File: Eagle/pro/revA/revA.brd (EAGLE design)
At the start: 100 x 100 mm, 4 parts

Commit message: mcu part
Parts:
- added U$1: ATSAM4LSAA-AUR, atmel:TQFP48
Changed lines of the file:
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@@
 <setting verticaltext="up"/>
 </settings>
-<grid distance="0.1" unitdist="mm" unit="mm" style="lines" multiple="1" display="yes" altdistance="0.025" altunitdist="inch" altunit="inch"/>
+<grid distance="0.1" unitdist="inch" unit="inch" style="lines" multiple="1" display="yes" altdistance="0.025" altunitdist="inch" altunit="inch"/>
 <layers>
 <layer number="1" name="Top" color="4" fill="1" visible="yes" active="yes"/>
@@
 <layer number="27" name="tValues" color="7" fill="1" visible="yes" active="yes"/>
 <layer number="28" name="bValues" color="7" fill="1" visible="yes" active="yes"/>
-<layer number="29" name="tStop" color="7" fill="3" visible="no" active="yes"/>
-<layer number="30" name="bStop" color="7" fill="6" visible="no" active="yes"/>
-<layer number="31" name="tCream" color="7" fill="4" visible="no" active="yes"/>
-<layer number="32" name="bCream" color="7" fill="5" visible="no" active="yes"/>
-<layer number="33" name="tFinish" color="6" fill="3" visible="no" active="yes"/>
-<layer number="34" name="bFinish" color="6" fill="6" visible="no" active="yes"/>
-<layer number="35" name="tGlue" color="7" fill="4" visible="no" active="yes"/>
-<layer number="36" name="bGlue" color="7" fill="5" visible="no" active="yes"/>
-<layer number="37" name="tTest" color="7" fill="1" visible="no" active="yes"/>
-<layer number="38" name="bTest" color="7" fill="1" visible="no" active="yes"/>
+<layer number="29" name="tStop" color="7" fill="3" visible="yes" active="yes"/>
+<layer number="30" name="bStop" color="7" fill="6" visible="yes" active="yes"/>
+<layer number="31" name="tCream" color="7" fill="4" visible="yes" active="yes"/>
+<layer number="32" name="bCream" color="7" fill="5" visible="yes" active="yes"/>
+<layer number="33" name="tFinish" color="6" fill="3" visible="yes" active="yes"/>
+<layer number="34" name="bFinish" color="6" fill="6" visible="yes" active="yes"/>
+<layer number="35" name="tGlue" color="7" fill="4" visible="yes" active="yes"/>
+<layer number="36" name="bGlue" color="7" fill="5" visible="yes" active="yes"/>
+<layer number="37" name="tTest" color="7" fill="1" visible="yes" active="yes"/>
+<layer number="38" name="bTest" color="7" fill="1" visible="yes" active="yes"/>
 <layer number="39" name="tKeepout" color="4" fill="11" visible="yes" active="yes"/>
 <layer number="40" name="bKeepout" color="1" fill="11" visible="yes" active="yes"/>
@@
 <layer number="42" name="bRestrict" color="1" fill="10" visible="yes" active="yes"/>
 <layer number="43" name="vRestrict" color="2" fill="10" visible="yes" active="yes"/>
-<layer number="44" name="Drills" color="7" fill="1" visible="no" active="yes"/>
+<layer number="44" name="Drills" color="7" fill="1" visible="yes" active="yes"/>
 <layer number="45" name="Holes" color="7" fill="1" visible="yes" active="yes"/>
-<layer number="46" name="Milling" color="3" fill="1" visible="no" active="yes"/>
-<layer number="47" name="Measures" color="7" fill="1" visible="no" active="yes"/>
+<layer number="46" name="Milling" color="3" fill="1" visible="yes" active="yes"/>
+<layer number="47" name="Measures" color="7" fill="1" visible="yes" active="yes"/>
 <layer number="48" name="Document" color="7" fill="1" visible="yes" active="yes"/>
 <layer number="49" name="Reference" color="7" fill="1" visible="yes" active="yes"/>
@@
 <element name="H3" library="holes" package="3,0-PAD" value="MOUNT-PAD-ROUND3.0" x="6" y="54"/>
 <element name="H4" library="holes" package="3,0-PAD" value="MOUNT-PAD-ROUND3.0" x="94" y="54"/>
+<element name="U$1" library="atmel" package="TQFP48" value="ATSAM4LSAA-AUR" x="27.8" y="17.1"/>
 </elements>
 <signals>

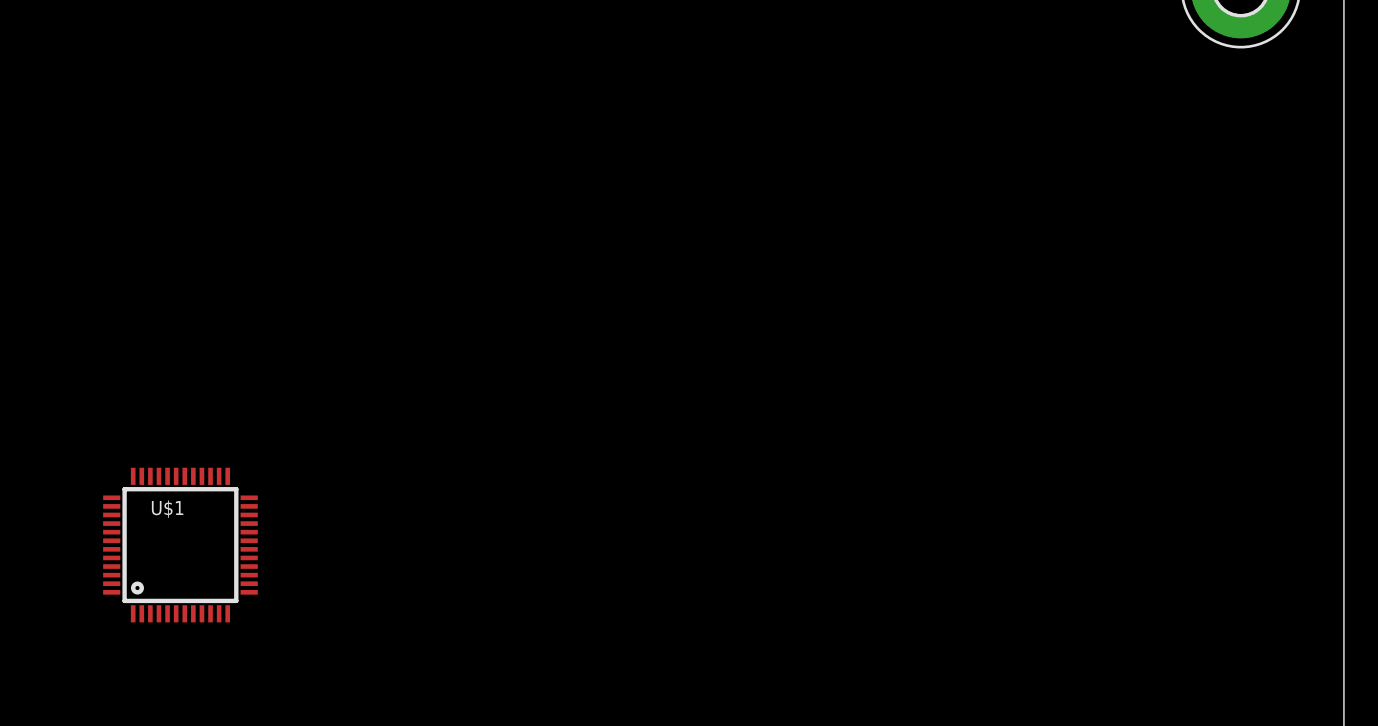
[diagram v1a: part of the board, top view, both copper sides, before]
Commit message: sort prog header
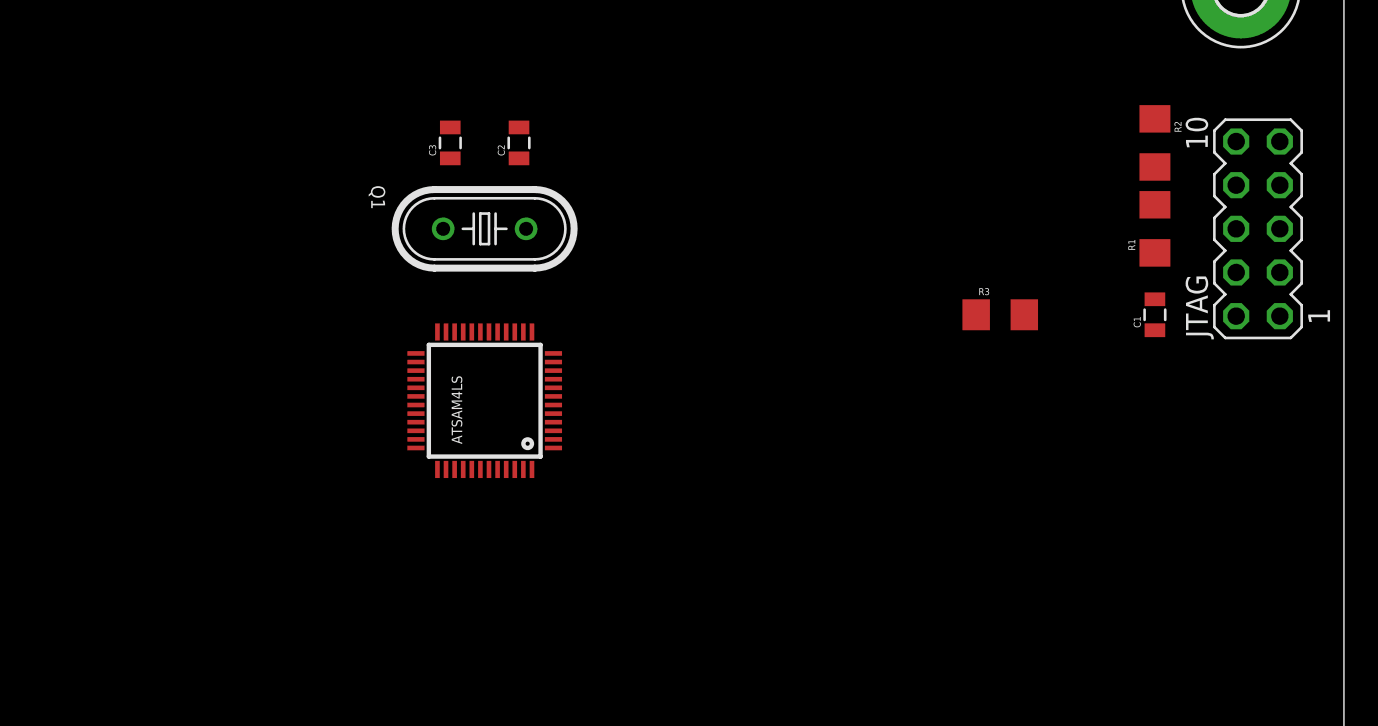
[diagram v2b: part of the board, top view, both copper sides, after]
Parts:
- removed U$1: ATSAM4LSAA-AUR, atmel:TQFP48
- added ATSAM4LS: ATSAM4LSAA-AUR, atmel:TQFP48
- added C1: 100nF, SparkFun:0805
- added C2, C3: 22pF, SparkFun:0805
- added JTAG: (no value), con-lstb:MA05-2
- added Q1: 20MHz, SparkFun:HC49U-V
- added R1, R2, R3: 100K, SparkFun:1206
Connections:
- new net 3.3V: C1.1, JTAG.1, R1.1, R2.1, R3.1
- new net GND: C1.2, C2.2, C3.2, JTAG.3, JTAG.5, JTAG.9
- new net N$1: ATSAM4LS.14, C3.1, Q1.2
- new net N$2: ATSAM4LS.13, C2.1, Q1.1
- new net NRESET: ATSAM4LS.4, JTAG.10
- new net TCK: ATSAM4LS.9, JTAG.4, R2.2
- new net TDI: ATSAM4LS.44, JTAG.8, R3.2
- new net TDO: ATSAM4LS.43, JTAG.6
- new net TMS: ATSAM4LS.10, JTAG.2, R1.2
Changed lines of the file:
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@@
 <setting verticaltext="up"/>
 </settings>
-<grid distance="0.1" unitdist="inch" unit="inch" style="lines" multiple="1" display="yes" altdistance="0.025" altunitdist="inch" altunit="inch"/>
+<grid distance="1" unitdist="mm" unit="mm" style="lines" multiple="1" display="yes" altdistance="0" altunitdist="inch" altunit="inch"/>
 <layers>
 <layer number="1" name="Top" color="4" fill="1" visible="yes" active="yes"/>
@@
 <layer number="48" name="Document" color="7" fill="1" visible="yes" active="yes"/>
 <layer number="49" name="Reference" color="7" fill="1" visible="yes" active="yes"/>
+<layer number="50" name="dxf" color="7" fill="1" visible="yes" active="yes"/>
 <layer number="51" name="tDocu" color="7" fill="1" visible="yes" active="yes"/>
 <layer number="52" name="bDocu" color="7" fill="1" visible="yes" active="yes"/>
+<layer number="53" name="tGND_GNDA" color="7" fill="9" visible="no" active="no"/>
+<layer number="54" name="bGND_GNDA" color="1" fill="9" visible="no" active="no"/>
+<layer number="56" name="wert" color="7" fill="1" visible="yes" active="yes"/>
 <layer number="91" name="Nets" color="2" fill="1" visible="no" active="no"/>
 <layer number="92" name="Busses" color="1" fill="1" visible="no" active="no"/>
@@
 <layer number="97" name="Info" color="7" fill="1" visible="no" active="no"/>
 <layer number="98" name="Guide" color="6" fill="1" visible="no" active="no"/>
+<layer number="100" name="Muster" color="7" fill="1" visible="no" active="no"/>
+<layer number="101" name="Patch_Top" color="12" fill="4" visible="yes" active="yes"/>
+<layer number="102" name="Vscore" color="7" fill="1" visible="yes" active="yes"/>
+<layer number="104" name="Name" color="7" fill="1" visible="yes" active="yes"/>
+<layer number="116" name="Patch_BOT" color="9" fill="4" visible="yes" active="yes"/>
+<layer number="121" name="_tsilk" color="7" fill="1" visible="yes" active="yes"/>
+<layer number="122" name="_bsilk" color="7" fill="1" visible="yes" active="yes"/>
+<layer number="151" name="HeatSink" color="7" fill="1" visible="yes" active="yes"/>
+<layer number="200" name="200bmp" color="1" fill="10" visible="yes" active="yes"/>
+<layer number="201" name="201bmp" color="2" fill="10" visible="yes" active="yes"/>
+<layer number="202" name="202bmp" color="3" fill="10" visible="yes" active="yes"/>
+<layer number="203" name="203bmp" color="4" fill="10" visible="yes" active="yes"/>
+<layer number="204" name="204bmp" color="5" fill="10" visible="yes" active="yes"/>
+<layer number="205" name="205bmp" color="6" fill="10" visible="yes" active="yes"/>
+<layer number="206" name="206bmp" color="7" fill="10" visible="yes" active="yes"/>
+<layer number="207" name="207bmp" color="8" fill="10" visible="yes" active="yes"/>
+<layer number="208" name="208bmp" color="9" fill="10" visible="yes" active="yes"/>
+<layer number="250" name="Descript" color="3" fill="1" visible="no" active="no"/>
+<layer number="251" name="SMDround" color="12" fill="11" visible="no" active="no"/>
+<layer number="254" name="cooling" color="7" fill="1" visible="yes" active="yes"/>
 </layers>
 <board>
@@
 <element name="H3" library="holes" package="3,0-PAD" value="MOUNT-PAD-ROUND3.0" x="6" y="54"/>
 <element name="H4" library="holes" package="3,0-PAD" value="MOUNT-PAD-ROUND3.0" x="94" y="54"/>
-<element name="U$1" library="atmel" package="TQFP48" value="ATSAM4LSAA-AUR" x="27.8" y="17.1"/>
+<element name="ATSAM4LS" library="atmel" package="TQFP48" value="ATSAM4LSAA-AUR" x="50" y="30" rot="R90"/>
+<element name="Q1" library="SparkFun" package="HC49U-V" value="20MHz" x="50" y="40" rot="R180"/>
+<element name="JTAG" library="con-lstb" package="MA05-2" value="" x="95" y="40" rot="R90">
+<attribute name="OC_NEWARK" value="unknown" x="95" y="40" size="1.778" layer="27" rot="R90" display="off"/>
+<attribute name="MPN" value="" x="95" y="40" size="1.778" layer="27" rot="R90" display="off"/>
+<attribute name="MF" value="" x="95" y="40" size="1.778" layer="27" rot="R90" display="off"/>
+<attribute name="OC_FARNELL" value="unknown" x="95" y="40" size="1.778" layer="27" rot="R90" display="off"/>
+</element>
+<element name="C1" library="SparkFun" package="0805" value="100nF" x="89" y="35" rot="R90"/>
+<element name="R1" library="SparkFun" package="1206" value="100K" x="89" y="40" rot="R90"/>
+<element name="R2" library="SparkFun" package="1206" value="100K" x="89" y="45" rot="R270"/>
+<element name="R3" library="SparkFun" package="1206" value="100K" x="80" y="35"/>
+<element name="C2" library="SparkFun" package="0805" value="22pF" x="52" y="45" rot="R90"/>
+<element name="C3" library="SparkFun" package="0805" value="22pF" x="48" y="45" rot="R90"/>
 </elements>
 <signals>
+<signal name="N$2">
+<contactref element="ATSAM4LS" pad="13"/>
+<contactref element="Q1" pad="1"/>
+<contactref element="C2" pad="1"/>
+<wire x1="52.413" y1="40" x2="52" y2="44.1" width="0" layer="19" extent="1-1"/>
+<wire x1="52.75290625" y1="33.9991125" x2="52.413" y2="40" width="0" layer="19" extent="1-1"/>
+</signal>
+<signal name="3.3V">
+<contactref element="R1" pad="1"/>
+<contactref element="R2" pad="1"/>
+<contactref element="JTAG" pad="1"/>
+<contactref element="C1" pad="1"/>
+<contactref element="R3" pad="1"/>
+<wire x1="89" y1="38.6" x2="89" y2="46.4" width="0" layer="19" extent="1-1"/>
+<wire x1="89" y1="34.1" x2="89" y2="38.6" width="0" layer="19" extent="1-1"/>
+<wire x1="96.27" y1="34.92" x2="89" y2="34.1" width="0" layer="19" extent="1-1"/>
+<wire x1="78.6" y1="35" x2="89" y2="34.1" width="0" layer="19" extent="1-1"/>
+</signal>
+<signal name="TMS">
+<contactref element="JTAG" pad="2"/>
+<contactref element="ATSAM4LS" pad="10"/>
+<contactref element="R1" pad="2"/>
+<wire x1="93.73" y1="34.92" x2="89" y2="41.4" width="0" layer="19" extent="1-1"/>
+<wire x1="54.00290625" y1="31.7491125" x2="89" y2="41.4" width="0" layer="19" extent="1-1"/>
+</signal>
+<signal name="TCK">
+<contactref element="JTAG" pad="4"/>
+<contactref element="R2" pad="2"/>
+<contactref element="ATSAM4LS" pad="9"/>
+<wire x1="93.73" y1="37.46" x2="89" y2="43.6" width="0" layer="19" extent="1-1"/>
+<wire x1="54.00290625" y1="31.2491125" x2="89" y2="43.6" width="0" layer="19" extent="1-1"/>
+</signal>
+<signal name="NRESET">
+<contactref element="ATSAM4LS" pad="4"/>
+<contactref element="JTAG" pad="10"/>
+<wire x1="54.00290625" y1="28.7491125" x2="93.73" y2="45.08" width="0" layer="19" extent="1-1"/>
+</signal>
+<signal name="TDO">
+<contactref element="JTAG" pad="6"/>
+<contactref element="ATSAM4LS" pad="43"/>
+<wire x1="50.25290625" y1="25.9991125" x2="93.73" y2="40" width="0" layer="19" extent="1-1"/>
+</signal>
+<signal name="TDI">
+<contactref element="JTAG" pad="8"/>
+<contactref element="ATSAM4LS" pad="44"/>
+<contactref element="R3" pad="2"/>
+<wire x1="81.4" y1="35" x2="93.73" y2="42.54" width="0" layer="19" extent="1-1"/>
+<wire x1="50.75290625" y1="25.9991125" x2="81.4" y2="35" width="0" layer="19" extent="1-1"/>
+</signal>
+<signal name="GND">
+<contactref element="C1" pad="2"/>
+<contactref element="JTAG" pad="5"/>
+<contactref element="JTAG" pad="9"/>
+<contactref element="JTAG" pad="3"/>
+<contactref element="C3" pad="2"/>
+<contactref element="C2" pad="2"/>
+<wire x1="96.27" y1="40" x2="96.27" y2="45.08" width="0" layer="19" extent="1-1"/>
+<wire x1="96.27" y1="37.46" x2="96.27" y2="40" width="0" layer="19" extent="1-1"/>
+<wire x1="89" y1="35.9" x2="96.27" y2="37.46" width="0" layer="19" extent="1-1"/>
+<wire x1="52" y1="45.9" x2="89" y2="35.9" width="0" layer="19" extent="1-1"/>
+<wire x1="48" y1="45.9" x2="52" y2="45.9" width="0" layer="19" extent="1-1"/>
+</signal>
+<signal name="N$1">
+<contactref element="Q1" pad="2"/>
+<contactref element="ATSAM4LS" pad="14"/>
+<contactref element="C3" pad="1"/>
+<wire x1="47.587" y1="40" x2="48" y2="44.1" width="0" layer="19" extent="1-1"/>
+<wire x1="52.25290625" y1="33.9991125" x2="47.587" y2="40" width="0" layer="19" extent="1-1"/>
+</signal>
 </signals>
 </board>

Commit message: op amps
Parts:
- added C4, C6: 22pF, SparkFun:0805
- added R10, R4, R6, R7, R8, R9: 100K, SparkFun:1206
- added U$1, U$2: LM393, SparkFun:SO08
- added U$3: AUDIO-JACKPTH, SparkFun:AUDIO-JACK
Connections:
- new net AUDIO_LEFT: ATSAM4LS.11, R4.2, U$1.1
- new net AUDIO_RIGHT: ATSAM4LS.12, R9.2, U$1.7
- new net N$10: U$1.4, U$2.4
- new net N$11: U$1.8, U$2.8
- new net N$12: U$2.3, U$3.2
- new net N$3: U$2.5, U$3.5
- new net N$4: R4.1, R6.2, U$1.2
- new net N$5: C6.1, R8.1, U$1.5
- new net N$6: C4.1, R7.1, U$1.3
- new net N$7: R8.2, U$2.6, U$2.7
- new net N$8: R7.2, U$2.1, U$2.2
- new net N$9: R10.2, R9.1, U$1.6
- net GND: now also C4.2, C6.2, R10.1, R6.1, U$3.1
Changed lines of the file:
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@@
 <element name="C2" library="SparkFun" package="0805" value="22pF" x="52" y="45" rot="R90"/>
 <element name="C3" library="SparkFun" package="0805" value="22pF" x="48" y="45" rot="R90"/>
+<element name="U$1" library="SparkFun" package="SO08" value="LM393" x="70" y="29"/>
+<element name="R4" library="SparkFun" package="1206" value="100K" x="55" y="16"/>
+<element name="R6" library="SparkFun" package="1206" value="100K" x="45" y="18"/>
+<element name="R7" library="SparkFun" package="1206" value="100K" x="78" y="16"/>
+<element name="C4" library="SparkFun" package="0805" value="22pF" x="73" y="14" rot="R90"/>
+<element name="R8" library="SparkFun" package="1206" value="100K" x="78" y="31"/>
+<element name="C6" library="SparkFun" package="0805" value="22pF" x="63" y="23"/>
+<element name="R9" library="SparkFun" package="1206" value="100K" x="67" y="41"/>
+<element name="R10" library="SparkFun" package="1206" value="100K" x="84" y="29" rot="R90"/>
+<element name="U$2" library="SparkFun" package="SO08" value="LM393" x="84" y="20"/>
+<element name="U$3" library="SparkFun" package="AUDIO-JACK" value="AUDIO-JACKPTH" x="95" y="20" rot="R180"/>
 </elements>
 <signals>
@@
 <contactref element="C3" pad="2"/>
 <contactref element="C2" pad="2"/>
+<contactref element="R6" pad="1"/>
+<contactref element="C4" pad="2"/>
+<contactref element="R10" pad="1"/>
+<contactref element="C6" pad="2"/>
+<contactref element="U$3" pad="1"/>
 <wire x1="96.27" y1="40" x2="96.27" y2="45.08" width="0" layer="19" extent="1-1"/>
 <wire x1="96.27" y1="37.46" x2="96.27" y2="40" width="0" layer="19" extent="1-1"/>
 <wire x1="89" y1="35.9" x2="96.27" y2="37.46" width="0" layer="19" extent="1-1"/>
-<wire x1="52" y1="45.9" x2="89" y2="35.9" width="0" layer="19" extent="1-1"/>
+<wire x1="95" y1="20" x2="89" y2="35.9" width="0" layer="19" extent="1-1"/>
+<wire x1="84" y1="27.6" x2="89" y2="35.9" width="0" layer="19" extent="1-1"/>
+<wire x1="63.9" y1="23" x2="84" y2="27.6" width="0" layer="19" extent="1-1"/>
+<wire x1="73" y1="14.9" x2="63.9" y2="23" width="0" layer="19" extent="1-1"/>
+<wire x1="43.6" y1="18" x2="73" y2="14.9" width="0" layer="19" extent="1-1"/>
+<wire x1="52" y1="45.9" x2="63.9" y2="23" width="0" layer="19" extent="1-1"/>
 <wire x1="48" y1="45.9" x2="52" y2="45.9" width="0" layer="19" extent="1-1"/>
 </signal>
@@
 <wire x1="52.25290625" y1="33.9991125" x2="47.587" y2="40" width="0" layer="19" extent="1-1"/>
 </signal>
+<signal name="AUDIO_RIGHT">
+<contactref element="ATSAM4LS" pad="12"/>
+<contactref element="U$1" pad="7"/>
+<contactref element="R9" pad="2"/>
+<wire x1="69.365" y1="31.6162" x2="68.4" y2="41" width="0" layer="19" extent="1-1"/>
+<wire x1="54.00290625" y1="32.7491125" x2="69.365" y2="31.6162" width="0" layer="19" extent="1-1"/>
+</signal>
+<signal name="AUDIO_LEFT">
+<contactref element="ATSAM4LS" pad="11"/>
+<contactref element="U$1" pad="1"/>
+<contactref element="R4" pad="2"/>
+<wire x1="54.00290625" y1="32.2491125" x2="68.095" y2="26.3838" width="0" layer="19" extent="1-1"/>
+<wire x1="56.4" y1="16" x2="68.095" y2="26.3838" width="0" layer="19" extent="1-1"/>
+</signal>
+<signal name="N$4">
+<contactref element="R4" pad="1"/>
+<contactref element="R6" pad="2"/>
+<contactref element="U$1" pad="2"/>
+<wire x1="53.6" y1="16" x2="69.365" y2="26.3838" width="0" layer="19" extent="1-1"/>
+<wire x1="46.4" y1="18" x2="53.6" y2="16" width="0" layer="19" extent="1-1"/>
+</signal>
+<signal name="N$6">
+<contactref element="C4" pad="1"/>
+<contactref element="U$1" pad="3"/>
+<contactref element="R7" pad="1"/>
+<wire x1="76.6" y1="16" x2="70.635" y2="26.3838" width="0" layer="19" extent="1-1"/>
+<wire x1="73" y1="13.1" x2="76.6" y2="16" width="0" layer="19" extent="1-1"/>
+</signal>
+<signal name="N$8">
+<contactref element="R7" pad="2"/>
+<contactref element="U$2" pad="2"/>
+<contactref element="U$2" pad="1"/>
+<wire x1="82.095" y1="17.3838" x2="83.365" y2="17.3838" width="0" layer="19" extent="1-1"/>
+<wire x1="79.4" y1="16" x2="82.095" y2="17.3838" width="0" layer="19" extent="1-1"/>
+</signal>
+<signal name="N$9">
+<contactref element="R10" pad="2"/>
+<contactref element="R9" pad="1"/>
+<contactref element="U$1" pad="6"/>
+<wire x1="70.635" y1="31.6162" x2="65.6" y2="41" width="0" layer="19" extent="1-1"/>
+<wire x1="84" y1="30.4" x2="70.635" y2="31.6162" width="0" layer="19" extent="1-1"/>
+</signal>
+<signal name="N$5">
+<contactref element="R8" pad="1"/>
+<contactref element="U$1" pad="5"/>
+<contactref element="C6" pad="1"/>
+<wire x1="71.905" y1="31.6162" x2="76.6" y2="31" width="0" layer="19" extent="1-1"/>
+<wire x1="62.1" y1="23" x2="71.905" y2="31.6162" width="0" layer="19" extent="1-1"/>
+</signal>
+<signal name="N$7">
+<contactref element="R8" pad="2"/>
+<contactref element="U$2" pad="7"/>
+<contactref element="U$2" pad="6"/>
+<wire x1="83.365" y1="22.6162" x2="79.4" y2="31" width="0" layer="19" extent="1-1"/>
+<wire x1="84.635" y1="22.6162" x2="83.365" y2="22.6162" width="0" layer="19" extent="1-1"/>
+</signal>
+<signal name="N$10">
+<contactref element="U$1" pad="4"/>
+<contactref element="U$2" pad="4"/>
+<wire x1="71.905" y1="26.3838" x2="85.905" y2="17.3838" width="0" layer="19" extent="1-1"/>
+</signal>
+<signal name="N$11">
+<contactref element="U$2" pad="8"/>
+<contactref element="U$1" pad="8"/>
+<wire x1="68.095" y1="31.6162" x2="82.095" y2="22.6162" width="0" layer="19" extent="1-1"/>
+</signal>
+<signal name="N$12">
+<contactref element="U$3" pad="2"/>
+<contactref element="U$2" pad="3"/>
+<wire x1="84.635" y1="17.3838" x2="90" y2="15" width="0" layer="19" extent="1-1"/>
+</signal>
+<signal name="N$3">
+<contactref element="U$3" pad="5"/>
+<contactref element="U$2" pad="5"/>
+<wire x1="85.905" y1="22.6162" x2="90" y2="25" width="0" layer="19" extent="1-1"/>
+</signal>
 </signals>
